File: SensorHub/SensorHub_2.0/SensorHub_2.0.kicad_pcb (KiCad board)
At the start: 4 copper layers, 30 x 28 mm, 67 parts, among them J2 658561423020, J3 658561423020, J5 FTSH-105-01-L-DV-K-A, J6 USB_C_Receptacle_USB2.0_16P, J8 USB_C_Receptacle_USB2.0_16P, SW1 SW_Push, SW2 SW_Push, U1 R7FA4E2B93CFM#AA0, U10 LMV339, U2 MYRGM080200C41RA, U3 TCAN334, U4 USBLC6-4SC6, U5 TMUX154EDGS, U6 LSM6DSM, U7 USBLC6-4SC6, Y1 ASH7KW-32.768KHZ-L-T

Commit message: PCB fix
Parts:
- removed C21: 0.1 uF, Capacitor_SMD:C_0603_1608Metric
- removed FRAME1: FRAME-LEDGER, SensorHub MicroMod Carrier v1.1.0b:CREATIVE_COMMONS
- removed J6, J8: USB_C_Receptacle_USB2.0_16P, Connector_USB:USB_C_Receptacle_Palconn_UTC16-G
- removed R10, R8, R9: 5.1 K, Resistor_SMD:R_0201_0603Metric
- removed R3: 100 K, Resistor_SMD:R_0201_0603Metric
- removed U10: LMV339, Package_SO:SOIC-14_3.9x8.7mm_P1.27mm
- removed U5: TMUX154EDGS, Package_SO:VSSOP-10_3x3mm_P0.5mm
- removed U7: USBLC6-4SC6, Package_TO_SOT_SMD:SOT-23-6
- added C5: 0.1 uF, Capacitor_SMD:C_0603_1608Metric, F.Cu at (140.0, 88.0)
- added J1: USB_C_Receptacle, Connector_USB:USB_C_Receptacle_Molex_105450-0101, F.Cu at (133.5, 82.8)
- added J4: USB_C_Receptacle, Connector_USB:USB_C_Receptacle_Molex_105450-0101, B.Cu at (133.5, 82.8)
- moved GP3 6.93 mm to (148.7, 83.4)
- moved GP2 6.29 mm to (148.7, 85.5)
- moved Res 3.14 mm to (141.4, 78.4)
- moved GND 2.40 mm to (148.7, 87.6)
- moved U4 1.98 mm to (140.0, 82.5), turned to 0 degrees
- moved C20 1.39 mm to (140.0, 86.4), turned to 0 degrees
- moved C7 0.91 mm to (148.4, 76.5)
- moved R4 0.91 mm to (147.8, 77.8)
- moved RES 0.91 mm to (144.8, 77.0)
- moved Boot 0.45 mm to (141.4, 76.3)
- moved Boot 0.34 mm to (144.9, 73.5)
- moved R5 0.34 mm to (143.6, 71.8)
- moved R6 0.34 mm to (146.2, 71.9)
- moved F1 0.10 mm to (139.6, 92.1)
- turned U$40 to 90 degrees
- renumbered SW2 to Boot, TP1 to Boot, TP10 to GND, TP7 to GP2, TP2 to GP3, SW1 to RES, TP5 to Res
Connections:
- J2 pad 2: +3.3V -> /+3.3V
- J3 pad 12: +3.3V -> /+3.3V
- U4 pad 1: /USB_DP -> /USB_DM
- U4 pad 3: /USB_DM -> /USB_DP
- U4 pad 4: /USB_C_2.0+SBUS/CC2 -> /Can_L
- U4 pad 6: /USB_C_2.0+SBUS/CC1 -> /Can_H
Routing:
- net /V_Bus: track 50.3 -> 18.5 mm, vias 2 -> 6
- net /USB_C_2.0+SBUS/SBU2: track 26.3 -> 0.00 mm, vias 4 -> 0
- net /USB_C_2.0+SBUS/SBU1: track 22.8 -> 0.00 mm, vias 3 -> 0
- net /USB_C_2.0+SBUS/CC1: track 20.6 -> 0.00 mm, vias 2 -> 0
- net /USB_C_2.0+SBUS/CC2: track 19.1 -> 0.00 mm, vias 2 -> 0
- net /Can_L: track 7.17 -> 24.3 mm, vias 1 -> 4
- net /USB_DM: track 36.4 -> 20.2 mm, vias 5 -> 4
- net Net-(U10D-+): track 13.9 -> 0.00 mm, vias 2 -> 0
- net GND: track 108.0 -> 95.1 mm, vias 42 -> 41
- net Net-(U10B-+): track 11.7 -> 0.00 mm, vias 2 -> 0
- net /Can_H: track 13.7 -> 24.2 mm, vias 3 -> 5
- net /USB_C_2.0+SBUS/EN: track 9.46 -> 0.00 mm, vias 2 -> 0
- net /RES: track 36.9 -> 28.6 mm, vias 3 -> 4
- net /USB_C_2.0+SBUS/cable_orient: track 8.25 -> 0.00 mm, vias 1 -> 0
- net /GP3: track 7.16 -> 2.88 mm, vias 1 -> 0
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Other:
- board text added: "Made on Earth"
- board text added: "RobotPatient.com"
- board text added: "SensorHub_2.0"

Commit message: Text fix
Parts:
- renumbered TP6 to EXTAL, Res to RES, TP4 to SCL, TP3 to SDA, TP8 to TXD
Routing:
- net /Can_L: track 24.3 -> 30.4 mm
- net /Can_H: track 24.2 -> 29.1 mm
- net GND: track 95.1 -> 97.8 mm, vias 41 -> 45
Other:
- board text added: "0.5\.1"
- board text added: "0.6\.1"
- board text added: "0.6\.15"
- board text added: "0.8\.15"

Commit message: Vesrion 2
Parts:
- removed the Boot at (144.9, 73.5)
- removed the Boot at (141.4, 76.3)
- removed D3: 1N4148WT, Diode_SMD:D_SOD-523
- removed EXTAL, TXD: TestPoint, TestPoint:TestPoint_THTPad_D1.0mm_Drill0.5mm
- removed the GND at (148.7, 87.6)
- removed J4: USB_C_Receptacle, Connector_USB:USB_C_Receptacle_Molex_105450-0101
- removed J5: FTSH-105-01-L-DV-K-A, FTSH-105-01-L-DV-K-A:SAMTEC_FTSH-105-01-L-DV-K-A
- removed R5: 1.5 K, Resistor_SMD:R_0201_0603Metric
- removed R6: 10 K, Resistor_SMD:R_0201_0603Metric
- removed the RES at (141.4, 78.4)
- removed the SCL at (167.0, 91.9)
- removed the SDA at (167.0, 93.9)
- added Boot: TestPoint, TestPoint:TestPoint_Pad_1.0x1.0mm, F.Cu at (147.9, 87.1)
- added C21: 0.1 uF, Capacitor_SMD:C_0603_1608Metric, F.Cu at (146.9, 73.4)
- added C22: 0.1 uF, Capacitor_SMD:C_0603_1608Metric, F.Cu at (146.3, 97.9)
- added C23: 0.1 uF, Capacitor_SMD:C_0603_1608Metric, F.Cu at (149.8, 97.8)
- added EXT: TestPoint, TestPoint:TestPoint_Pad_1.0x1.0mm, F.Cu at (156.9, 75.5)
- added GND: TestPoint, TestPoint:TestPoint_Pad_1.0x1.0mm, F.Cu at (142.8, 78.9)
- added J6: USB_C_Receptacle_USB2.0_16P, Connector_USB:USB_C_Receptacle_Palconn_UTC16-G, B.Cu at (155.0, 67.0)
- added J8: USB_C_Receptacle_USB2.0_16P, Connector_USB:USB_C_Receptacle_Palconn_UTC16-G, F.Cu at (155.0, 67.0)
- added R10: 5.1 K, Resistor_SMD:R_0201_0603Metric, B.Cu at (161.1, 75.7)
- added R16: 10k, Resistor_SMD:R_0201_0603Metric, F.Cu at (162.7, 72.0)
- added R3: 100 K, Resistor_SMD:R_0201_0603Metric, B.Cu at (154.8, 81.7)
- added R8: 5.1 K, Resistor_SMD:R_0201_0603Metric, B.Cu at (153.4, 81.7)
- added R9: 5.1 K, Resistor_SMD:R_0201_0603Metric, B.Cu at (161.1, 77.2)
- added RES: TestPoint, TestPoint:TestPoint_Pad_1.0x1.0mm, F.Cu at (147.9, 84.9)
- added RXD: TestPoint, TestPoint:TestPoint_Pad_1.0x1.0mm, F.Cu at (168.5, 76.2)
- added SCL: TestPoint, TestPoint:TestPoint_Pad_1.0x1.0mm, F.Cu at (160.5, 91.8)
- added SDA: TestPoint, TestPoint:TestPoint_Pad_1.0x1.0mm, F.Cu at (163.6, 97.5)
- added U10: LMV339, Package_SO:SOIC-14_3.9x8.7mm_P1.27mm, B.Cu at (156.0, 75.7)
- added U5: USBLC6-4SC6, Package_TO_SOT_SMD:SOT-23-6, B.Cu at (160.1, 89.7)
- added U7: USBLC6-4SC6, Package_TO_SOT_SMD:SOT-23-6, F.Cu at (157.9, 72.8)
- added U8: USBLC6-4SC6, Package_TO_SOT_SMD:SOT-23-6, B.Cu at (152.9, 89.3)
- added U9: USBLC6-4SC6, Package_TO_SOT_SMD:SOT-23-6, F.Cu at (146.4, 94.3)
- C4, R13, R14, R15, R7, U3: moved to F.Cu
- GP2, GP3: footprint TestPoint:TestPoint_THTPad_D1.0mm_Drill0.5mm -> TestPoint:TestPoint_Pad_1.0x1.0mm
- J1: value USB_C_Receptacle -> Conn_01x04_Pin; footprint Connector_USB:USB_C_Receptacle_Molex_105450-0101 -> Connector_PinHeader_1.27mm:PinHeader_1x04_P1.27mm_Vertical
- moved C5 23.0 mm to (161.0, 97.3)
- moved J1 18.7 mm to (149.7, 92.0), turned to 0 degrees
- moved C9 18.4 mm to (165.9, 78.0), turned to 180 degrees
- moved U6 17.7 mm to (162.0, 94.6), turned to 90 degrees
- moved R15 17.5 mm to (160.0, 95.7)
- moved D4 17.0 mm to (165.9, 80.3), turned to -90 degrees
- moved C20 16.2 mm to (146.9, 71.8), turned to 180 degrees
- moved C15 16.1 mm to (165.9, 85.8), turned to 180 degrees
- moved D5 16.0 mm to (165.9, 83.5), turned to 180 degrees
- moved F1 16.0 mm to (142.9, 76.4), turned to 0 degrees
- moved R7 15.4 mm to (160.0, 93.6), turned to -90 degrees
- moved C8 14.4 mm to (164.4, 94.9), turned to 90 degrees
- moved U4 14.2 mm to (150.9, 73.4)
- moved R13 12.8 mm to (164.5, 72.3), turned to 180 degrees
- moved R14 12.4 mm to (164.5, 73.9), turned to 180 degrees
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- renumbered RES to SW1
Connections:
- C5 pad 1: /V_Bus -> +3.3V
- F1 pad 1: Net-(D3-A) -> +5V
- J2 pad 2: /+3.3V -> +3.3V
- J3 pad 12: /+3.3V -> +3.3V
- U1 pad 1: /INT1 -> unconnected-(U1-P400-Pad1)
- U1 pad 14: /GP1 -> unconnected-(U1-P409-Pad14)
- U1 pad 2: /SCL_0 -> /TXD
- U1 pad 21: unconnected-(U1-CACREF-Pad21) -> /GP3
- U1 pad 22: unconnected-(U1-P206-Pad22) -> /GP2
- U1 pad 27: /RA4E2_microcontroller/LED -> unconnected-(U1-P200-Pad27)
- U1 pad 29: /GP3 -> unconnected-(U1-P303-Pad29)
- U1 pad 3: unconnected-(U1-CACREF-Pad3) -> /RXD
- U1 pad 30: /GP2 -> unconnected-(U1-P302-Pad30)
- U1 pad 4: /SDA_0 -> unconnected-(U1-P403-Pad4)
- U1 pad 44: /INT2 -> unconnected-(U1-P104-Pad44)
- U1 pad 47: /TXD -> /SDA_0
- U1 pad 48: /RXD -> /SCL_0
- U1 pad 49: unconnected-(U1-CACREF-Pad49) -> /GP1
- U1 pad 50: unconnected-(U1-P008-Pad50) -> /INT2
- U1 pad 51: unconnected-(U1-P006-Pad51) -> /INT1
- U1 pad 54: unconnected-(U1-P013-Pad54) -> /RA4E2_microcontroller/LED
- U3 pad 5: GND -> Net-(U3-SHDN)
- U3 pad 8: GND -> /EN
- U4 pad 1: /USB_DM -> /USB_DP
- U4 pad 3: /USB_DP -> /USB_DM
- U4 pad 4: /Can_L -> /USB_C_2.0+SBUS/CC1
- U4 pad 6: /Can_H -> /USB_C_2.0+SBUS/CC2
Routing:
- net /V_Bus: track 18.5 -> 66.1 mm, vias 6 -> 2
- net +3.3V: track 39.4 -> 68.9 mm, vias 17 -> 13
- net /RES: track 28.6 -> 7.09 mm, vias 4 -> 0
- net /USB_C_2.0+SBUS/CC1: track 0.00 -> 21.3 mm, vias 0 -> 2
- net /USB_C_2.0+SBUS/CC2: track 0.00 -> 20.8 mm, vias 0 -> 2
- net GND: track 97.8 -> 79.1 mm, vias 45 -> 41
- net /SCL_0: track 34.1 -> 15.6 mm, vias 2 -> 1
- net /Can_H: track 29.1 -> 13.0 mm, vias 5 -> 1
- net /RA4E2_microcontroller/Boot: track 19.5 -> 4.15 mm
- net Net-(U10A-+): track 0.00 -> 14.4 mm
- net +5V: track 28.2 -> 41.2 mm, vias 2 -> 3
- net /SDA_0: track 36.5 -> 24.0 mm, vias 4 -> 1
- net Net-(U10D-+): track 0.00 -> 12.4 mm
- net /Can_L: track 30.4 -> 18.1 mm, vias 4 -> 1
- net /TXD: track 15.0 -> 2.95 mm, vias 1 -> 0
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- added copper zone on B.Cu, net GND
- added copper zone on F.Cu, net GND
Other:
- board size 30 x 28 mm -> 30 x 37.3 mm
- board text added: "CAN Pull-Up R13,R14,C4 (optional)"
- board text removed: "0.5\.1"
- board text removed: "0.6\.1"
- board text removed: "0.6\.15"
- board text removed: "0.8\.15"

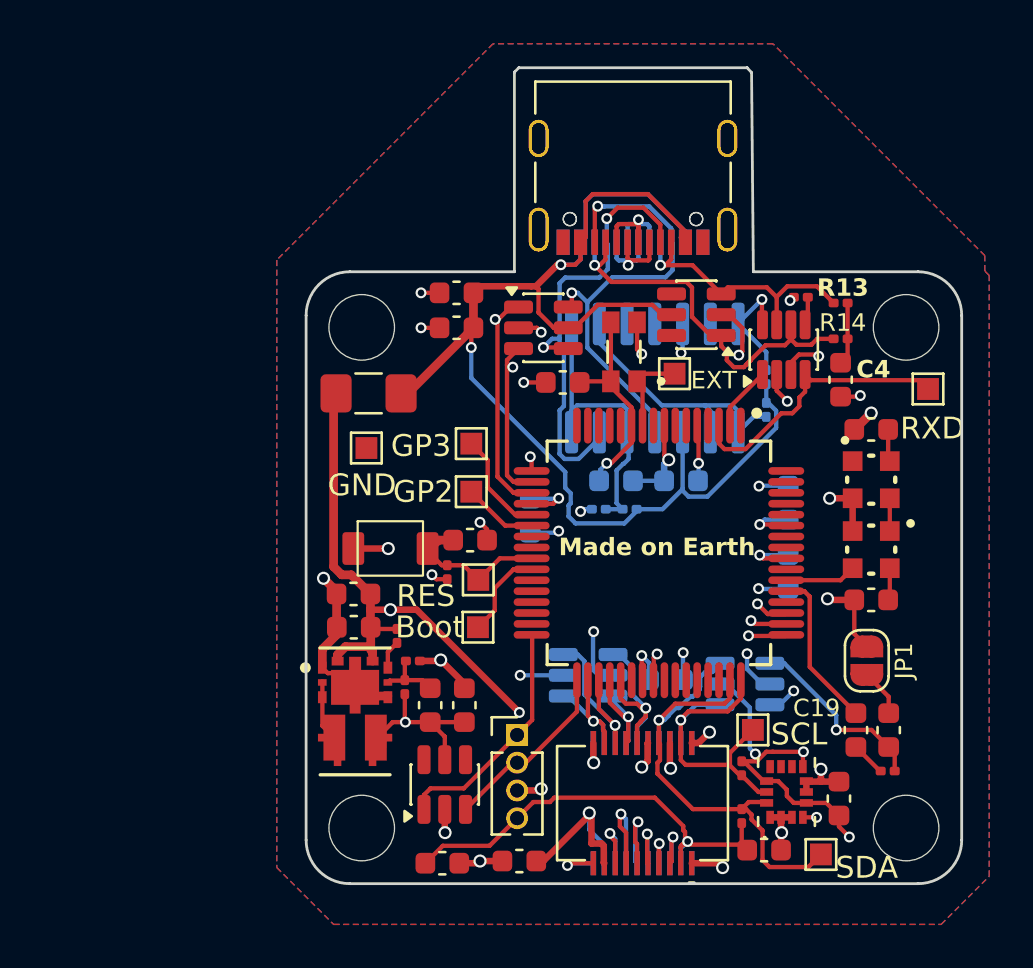
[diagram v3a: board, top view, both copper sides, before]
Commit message: MPN + CC fix
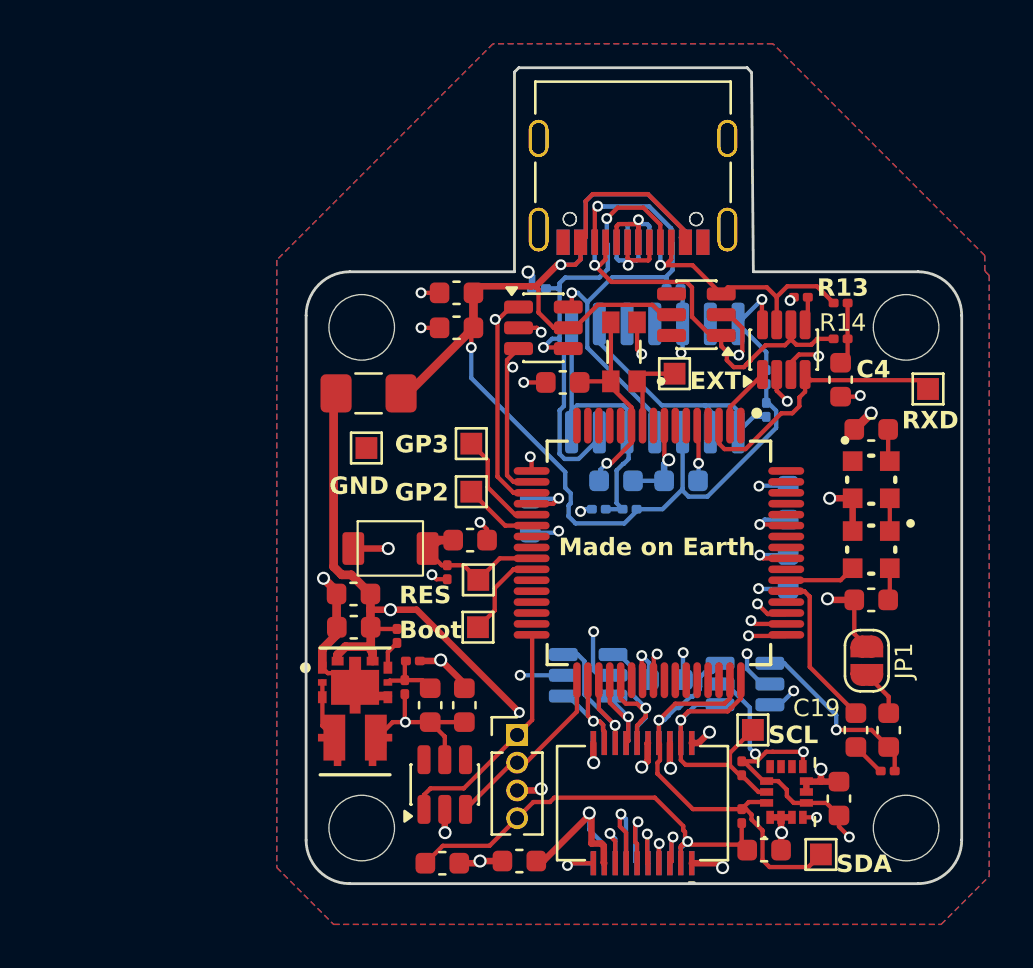
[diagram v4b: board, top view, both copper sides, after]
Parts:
- added R5: 5.1 K, Resistor_SMD:R_0201_0603Metric, B.Cu at (156.9, 71.6)
- added R6: 5.1 K, Resistor_SMD:R_0201_0603Metric, B.Cu at (150.7, 71.6)
- D4, D5: value 1312020030000 -> LED
- renumbered Boot to TP1, GND to TP10, GP3 to TP2, SDA to TP3, SCL to TP4, RES to TP5, EXT to TP6, GP2 to TP7, RXD to TP8
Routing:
- net GND: track 79.1 -> 81.6 mm, vias 41 -> 42
- net /USB_C_2.0+SBUS/CC1: track 21.3 -> 21.9 mm
- net /USB_C_2.0+SBUS/CC2: track 20.8 -> 21.3 mm
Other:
- board text added: "Boot"
- board text added: "EXT"
- board text added: "GND"
- board text added: "GP2"
- board text added: "GP3"
- board text added: "RES"
- board text added: "RXD"
- board text added: "SCL"
- board text added: "SDA"
